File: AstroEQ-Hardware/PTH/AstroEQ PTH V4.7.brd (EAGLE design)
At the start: 100 x 66 mm, 52 parts, among them IC1 ATMEGA162-16PU-SKT, IC2 PIC18F14K50-I/P-SKT, IC3 78L05, M1 Motor Driver, M2 Motor Driver, Q1 NTR4501NT1G, X1 16MHz, X2 12MHz

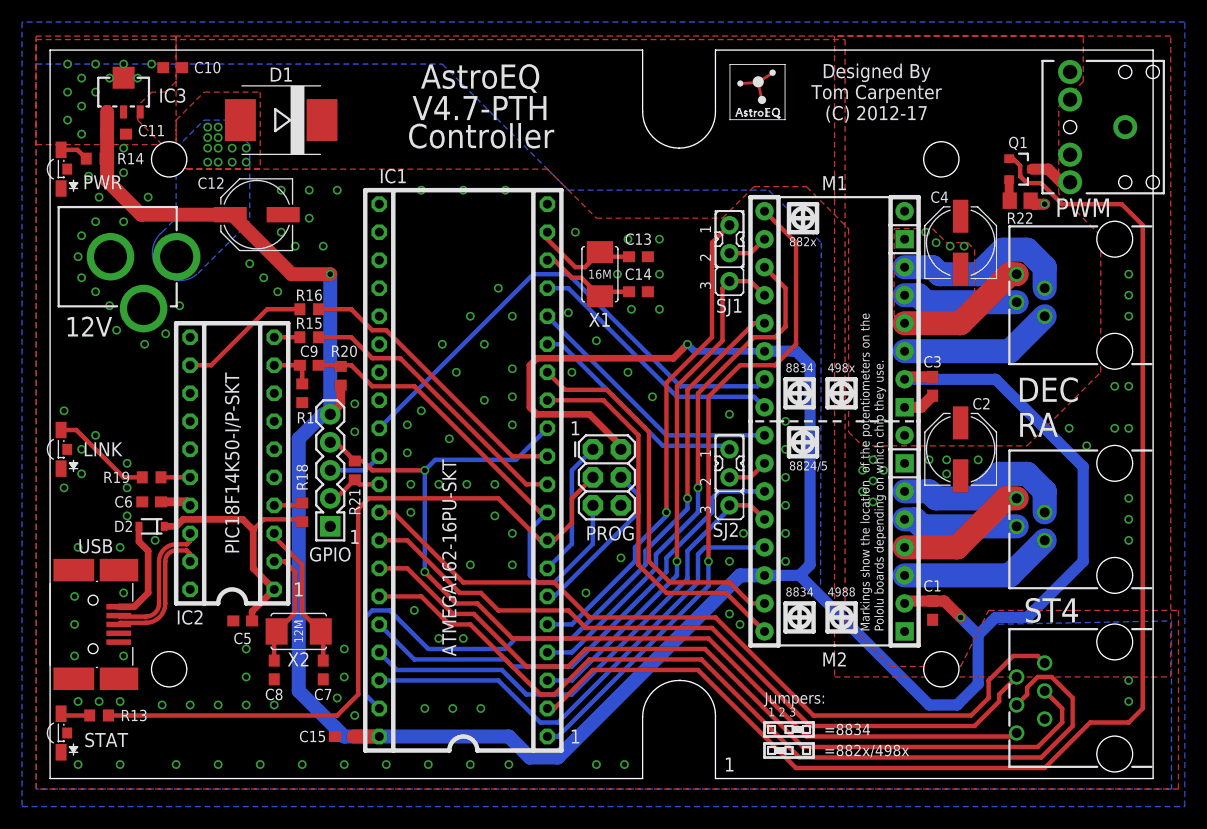
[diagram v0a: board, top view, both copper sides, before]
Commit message: Update Hardware Designs
Minor corrections to part attributes and some components in the V4.7
design moved slightly to avoid collisions as found during the prototype
build.
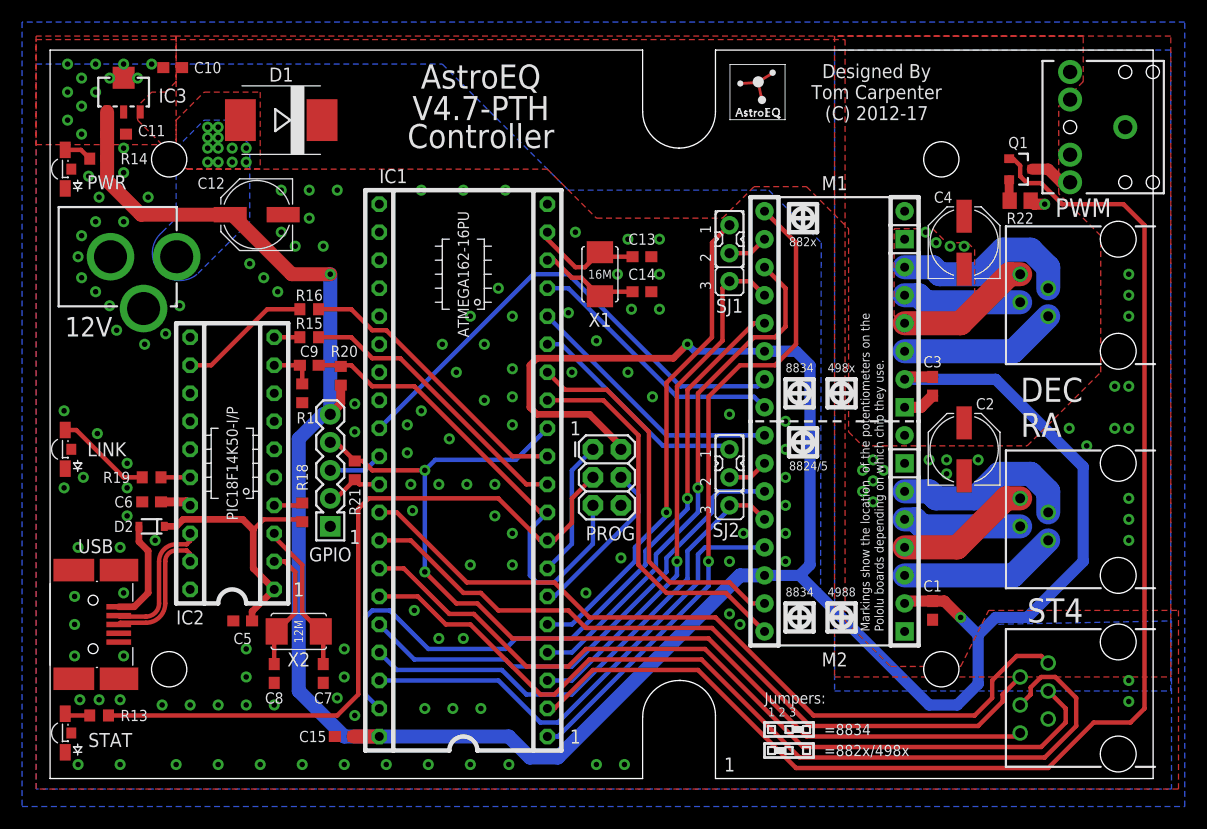
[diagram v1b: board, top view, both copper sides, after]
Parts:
- added ICL1: ATMEGA162-16PU, ic-package:IC
- added ICL2: PIC18F14K50-I/P, ic-package:IC
- D2: value PMEG2010EA -> RB511VM-30FHTE-17
- GPIO, J2, J3: value (none) -> DNI
- IC1: value ATMEGA162-16PU-SKT -> DIP40-SOCKET
- IC2: value PIC18F14K50-I/P-SKT -> DIP20-SOCKET
- LOGO1: value ASTROEQ5MM -> DNI
- SJ1, SJ2: value (none) -> 3pin HDR
- moved LINK 0.38 mm to (1.38, 29.8)
- moved PWR 0.38 mm to (1.38, 55.2)
- moved STAT 0.38 mm to (1.38, 4.13)
- moved C2 0.32 mm to (82.9, 29.8)
- moved C4 0.32 mm to (82.9, 48.6)
- moved DEC 0.32 mm to (96.8, 43.8)
- moved RA 0.32 mm to (96.8, 23.5)
- moved ST4 0.32 mm to (96.8, 7.30)
- moved R14 0.32 mm to (4.45, 56.2)
- moved C7 0.32 mm to (24.8, 9.53)
- moved C8 0.32 mm to (20.3, 9.53)
- moved C13 0.32 mm to (53.7, 47.3)
- moved C14 0.32 mm to (53.7, 44.1)
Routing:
- net GND: vias 169 -> 168
